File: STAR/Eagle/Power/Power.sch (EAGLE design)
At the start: 24 parts, among them J1 J30J-9J30, T1 750311838, U1 LT8300, U2 LT8330

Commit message: Power Board
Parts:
- removed D4: PMEG6010CEJ, AR_diode:SCHOTTKYSOD323
- removed T1: 750311838, AR_transformer:750311838
- added C10, C11, C12: .18 uF, resistor:C-USC0603
- added C13, C14, C15: 10 uF, resistor:C-USC0603
- added C16, C18, C20, C22, C24: KTJ500B476M76BFT00, Filtering:KTJ500B476M76BFT00
- added C17, C19, C21, C23, C25: 1nF, resistor:C-USC0603
- added C8, C9: .1 uF, resistor:C-USC0603
- added L2: 5.5u, Filtering:744325550
- added L3: 3.7u, Power:7443551370
- added L4, L5, L6, L7, L8: 744029000068, Filtering:744029000068
- added R9: 13.3k, resistor:R-US_R0603
- added U$1, U$2: DFT7160-105B, Filtering:DFT7160-105B
- added U3: LMR16020, HASP:LMR16020
- C1: value 22uF -> 10 uF; device AR_passives:CAPACITORC3025 -> resistor:C-USC1210
- C2: value 1uF -> 10 uF; device AR_passives:CAPACITORC0603 -> resistor:C-USC1210
- C3: value (none) -> 10 uF
- C4: value 10uF -> 2.2 uF; device AR_passives:CAPACITOR2-J-LEAD -> resistor:C-USC1210
- C5: value 1uF -> 2.2 uF; device AR_passives:CAPACITORC0603 -> resistor:C-USC1210
- C6: value 4.7pF -> 2.2 uF; device AR_passives:CAPACITORC0603 -> resistor:C-USC1210
- C7: value 1uF -> .1 uF; device AR_passives:CAPACITORC0603 -> resistor:C-USC0603
- D1: value MMSZ5266BT1G -> DO-214AC; device AR_diode:ZENERSOD123 -> HASP:DO-214AC
- D2: value BAV20W -> DO-214AC; device AR_diode:SCHOTTKYSOD323 -> HASP:DO-214AC
- D3: value SBR0560S1 -> DO-214AC; device AR_diode:SCHOTTKYSOD123 -> HASP:DO-214AC
- J1: value J30J-9J30 -> J30J-25; device CM_J30J:J30J-9J30 -> CM_J30J:J30J-25
- L1: value 10uH -> 9.7u; device AR_passives:INDUCTORPQ2614 -> Power:744314101
- R1: value 47k -> 23.2k; device resistor:R-US_R2512 -> resistor:R-US_R0603
- R2: value 407k -> 23.2k
- R3: value 1k -> 23.2k
- R4: value 3k -> 199.5k; device resistor:R-US_R2512 -> resistor:R-US_R0603
- R5: value 1.5k -> 13.3k; device resistor:R-US_R2512 -> resistor:R-US_R0603
- R6: value 1M -> 75.4k
- R7: value 33k -> 13.3k
- R8: value 52.6 -> 45.2k
- U1: value LT8300 -> LMR16020; device AR_IC:LT8300 -> HASP:LMR16020
- U2: value LT8330 -> LMR16020; device AR_IC:LT8330 -> HASP:LMR16020
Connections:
- removed net +20V: C3.1, C5.1, D3.C, L1.1, U2.EN, U2.VCC
- removed net +50V: C4.1, C6.1, D4.C, J1.1, J1.2, R1.2, R5.2, R6.2
- removed net N$11: R7.1, R8.2
- removed net VCC: C1.1, C2.1, D1.A, J1.4, T1.PA, U1.EN, U1.VCC
- removed net V_DIVIDE: J1.5, R1.1, R4.2
- new net +12V: C10.1, C13.1, L1.P$2, L8.P$1, R4.2
- new net +3V3: C12.1, C15.1, L3.P$2, L6.P$1, R8.2
- new net +5V: C11.1, C14.1, L2.P$2, L5.P$1, R6.2
- new net 12V_FILT: C24.P$1, C25.1, J1.3, L8.P$2
- new net 3V3_FILT: C20.P$1, C21.1, J1.1, L6.P$2
- new net 5V_FILT: C18.P$1, C19.1, J1.16, J1.18, J1.2, J1.8, L5.P$2
- new net D: J1.10
- new net ER: J1.12
- new net F: J1.6
- new net GSE_FILT: C16.P$1, C17.1, C2.1, C3.1, C5.1, C6.1, L4.P$2, U2.EN, U2.VIN, U3.EN, U3.VIN
- new net GSE_GND: C11.2, C12.2, C14.2, C15.2, C16.P$2, C17.2, C18.P$2, C19.2, C2.2, C20.P$2, C21.2, C3.2, C5.2, C6.2, D2.P$1, D3.P$1, J1.14, J1.17, J1.19, J1.20, J1.21, J1.22, R2.1, R3.1, R7.1, R9.1, U2.GND, U3.GND
- new net GSE_UFILT: J1.15, U$1.P$1, U$1.P$3
- new net I: J1.4
- new net N$14: C7.1, D1.P$2, L1.P$1, U1.SW
- new net N$27: R4.1, R5.2, U1.FB
- new net N$28: L4.P$1, U$1.P$2, U$1.P$4
- new net N$29: L7.P$1, U$2.P$2, U$2.P$4
- new net N$44: J1.25
- new net N$45: J1.24
- new net N$46: J1.23
- new net N$8: R8.1, R9.2, U3.FB
- new net Q: J1.7
- new net T: J1.5
- new net TE_FILT: C1.1, C22.P$1, C23.1, C4.1, L7.P$2, U1.EN, U1.VIN
- new net TE_UFILT: J1.13, U$2.P$1, U$2.P$3
- net GND: now also C10.2, C13.2, C22.P$2, C23.2, C24.P$2, C25.2, D1.P$1, J1.11, J1.9, R1.1; no longer C2.2, C3.2, C5.2, C7.2, J1.6, J1.7, R4.1, R8.1, T1.S2A, U2.GND
- net N$1: now also R3.2, U3.RT/SYNC; no longer D1.C, D2.C
- net N$10: now also C7.2, U1.BOOT; no longer J1.9
- net N$2: now also C9.1, D3.P$2, L3.P$1, U3.SW; no longer R2.1, U1.FB
- net N$3: now also U2.RT/SYNC; no longer R3.1
- net N$4: now also C8.2, U2.BOOT; no longer D2.A, R3.2, T1.PB, U1.SW
- net N$5: now also C8.1, D2.P$2, L2.P$1, U2.SW; no longer D3.A, T1.S2B
- net N$6: now also C9.2, U3.BOOT; no longer C7.1, U2.INTVCC
- net N$7: now also R1.2, U1.RT/SYNC; no longer D4.A, L1.2, U2.SW
- net N$9: no longer C6.2
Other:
- note added: "12 V Line"
- note added: "3.3 V Line"
- note added: "5 V Line"
- note added: "GSE Filter Network"
- note added: "TE Filter Network"
- note removed: "BOOST STAGE"
- note removed: "ISOLATION STAGE"
- note removed: "Voltage Divider"
- moved on the sheet: C1, C2, C3, C4, C5, C6, C7, R1, R2, R3, R4, R5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

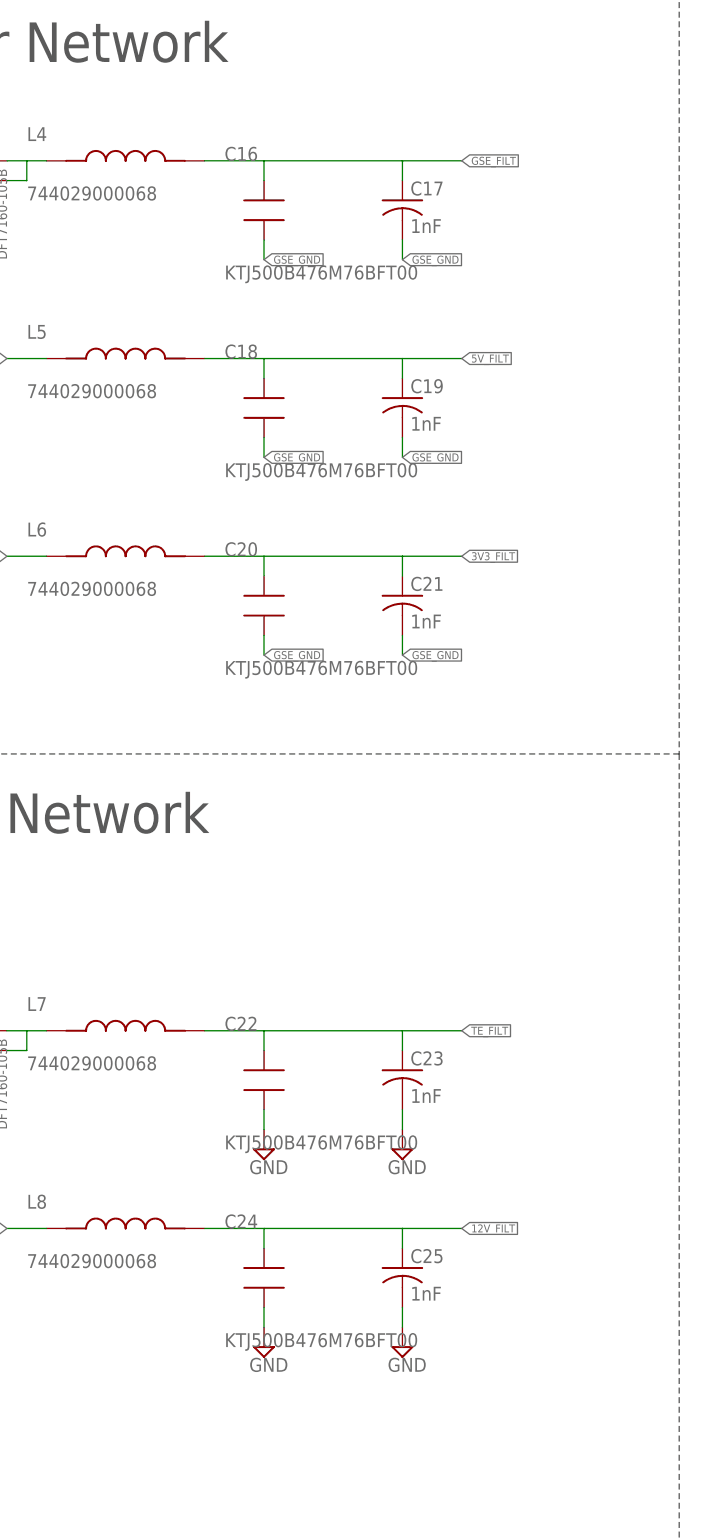
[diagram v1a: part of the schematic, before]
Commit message: new filtering caps for power board
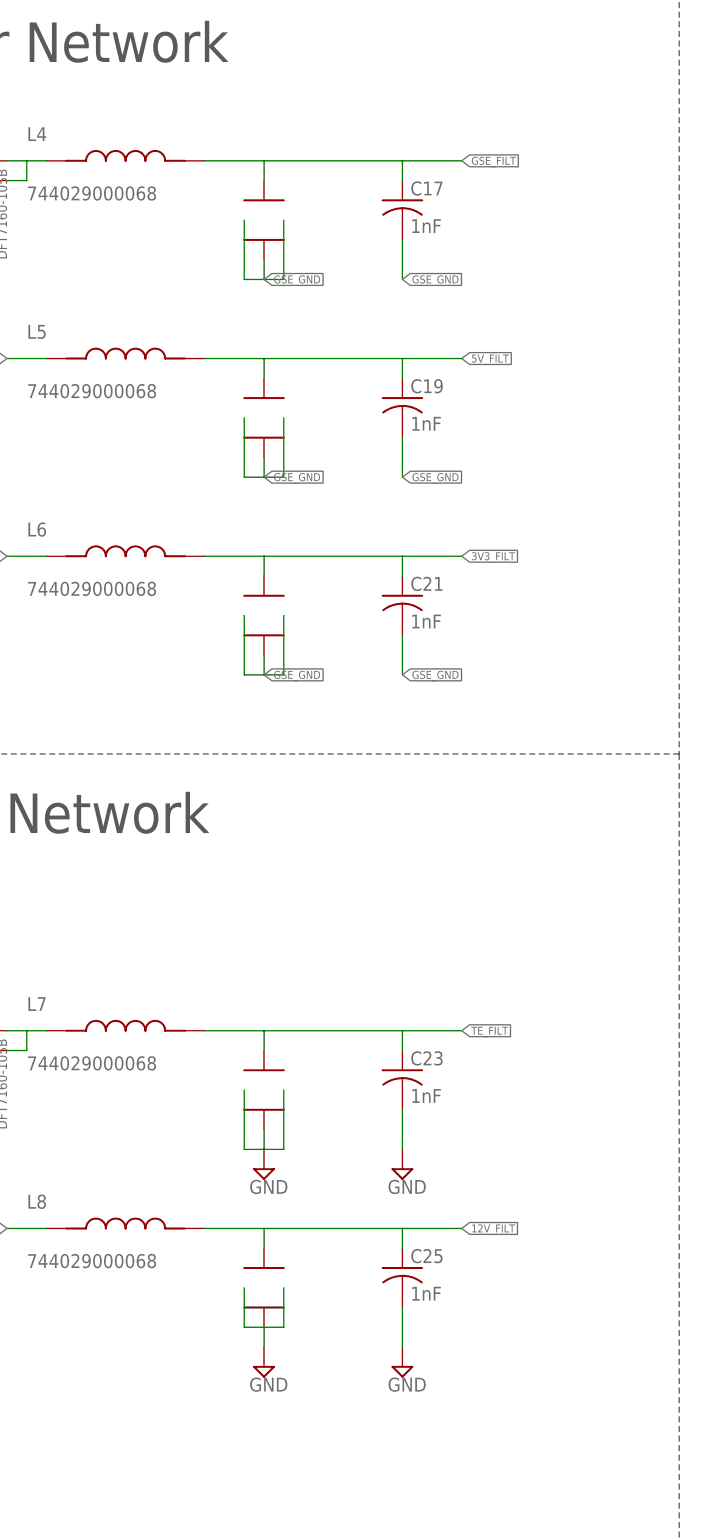
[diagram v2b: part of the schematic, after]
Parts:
- removed C16, C18, C20, C22, C24: KTJ500B476M76BFT00, Filtering:KTJ500B476M76BFT00
- added U$3, U$4, U$5, U$6, U$7: 1410J0500404MXTE03, Filtering:1410J0500404MXTE03
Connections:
- net 12V_FILT: now also U$7.P$2; no longer C24.P$1
- net 3V3_FILT: now also U$5.P$2; no longer C20.P$1
- net 5V_FILT: now also U$4.P$2; no longer C18.P$1
- net GND: now also U$6.P$1, U$6.P$3, U$6.P$4, U$7.P$1, U$7.P$3, U$7.P$4; no longer C22.P$2, C24.P$2
- net GSE_FILT: now also U$3.P$2; no longer C16.P$1
- net GSE_GND: now also U$3.P$1, U$3.P$3, U$3.P$4, U$4.P$1, U$4.P$3, U$4.P$4, U$5.P$1, U$5.P$3, U$5.P$4; no longer C16.P$2, C18.P$2, C20.P$2
- net TE_FILT: now also U$6.P$2; no longer C22.P$1

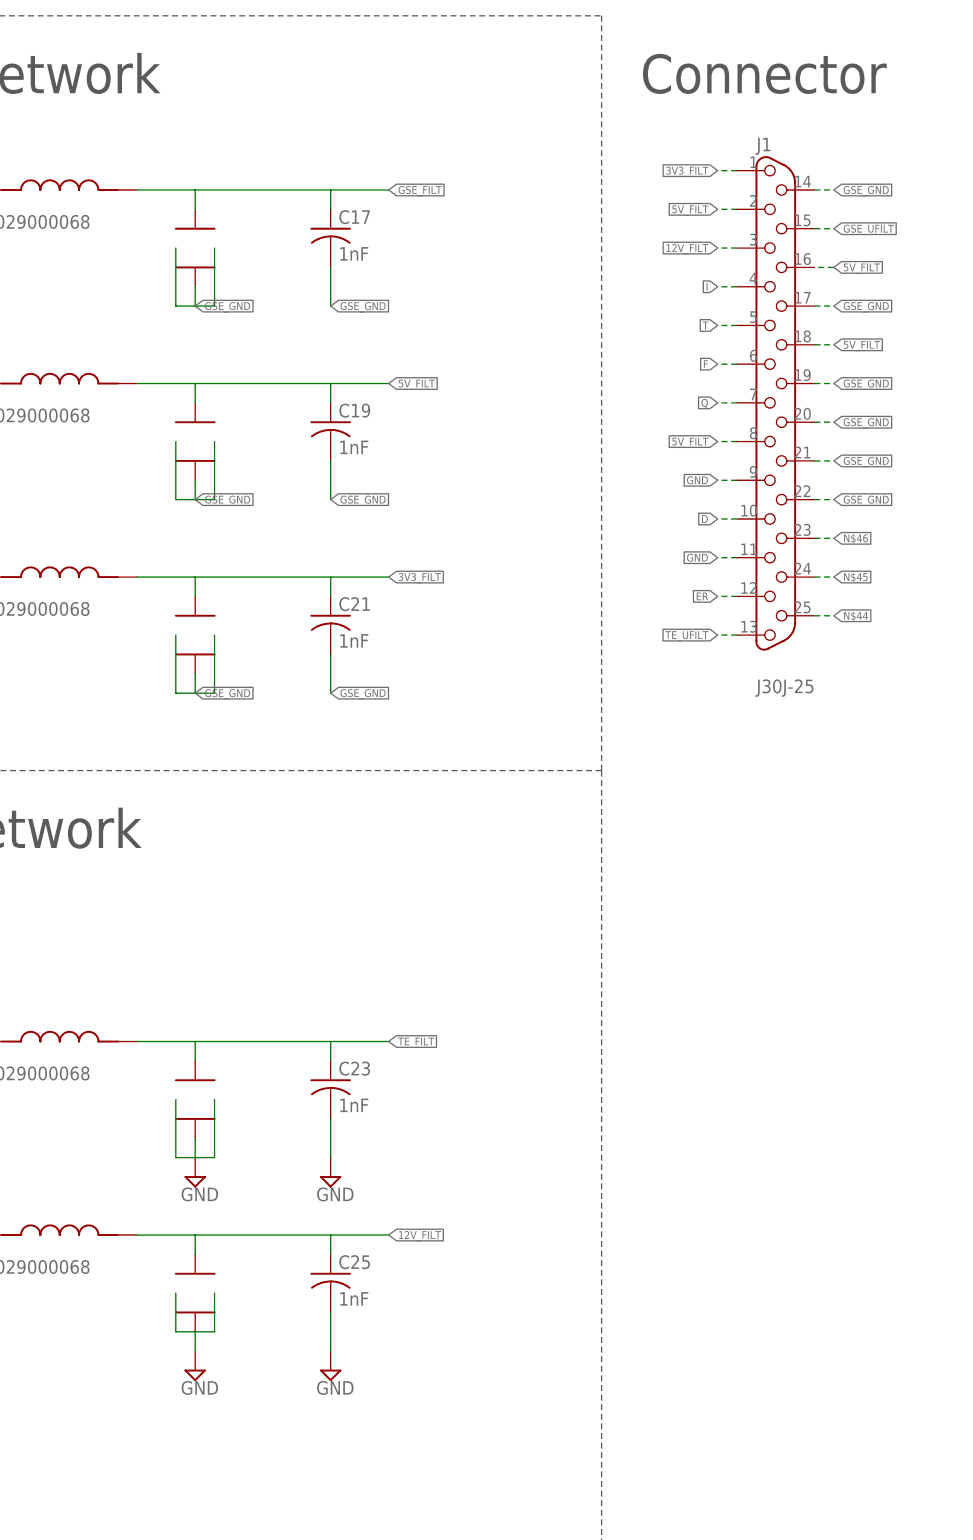
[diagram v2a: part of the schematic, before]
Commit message: Fixed the three terminal capacitor routing (five capacitors).
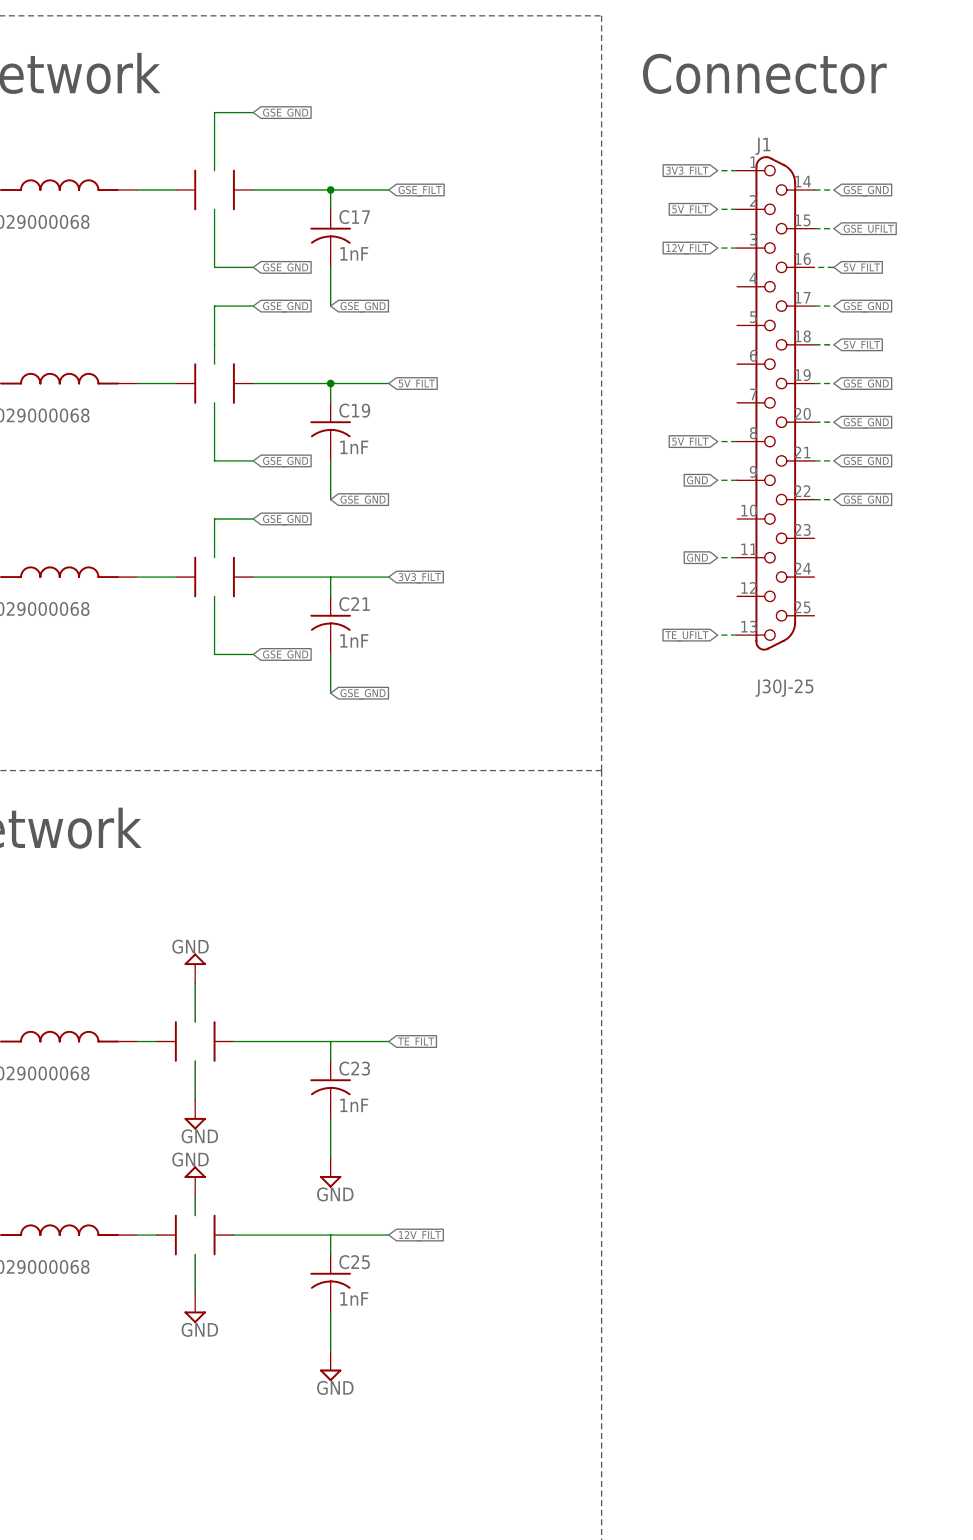
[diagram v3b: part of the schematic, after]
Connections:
- removed net D: J1.10
- removed net ER: J1.12
- removed net F: J1.6
- removed net I: J1.4
- removed net N$44: J1.25
- removed net N$45: J1.24
- removed net N$46: J1.23
- removed net Q: J1.7
- removed net T: J1.5
- new net N$31: L4.P$2, U$3.P$2
- new net N$32: L5.P$2, U$4.P$2
- new net N$33: L6.P$2, U$5.P$1
- new net N$34: L7.P$2, U$6.P$1
- new net N$35: L8.P$2, U$7.P$1
- net 12V_FILT: no longer L8.P$2
- net 3V3_FILT: no longer L6.P$2
- net 5V_FILT: now also U$4.P$1; no longer L5.P$2, U$4.P$2
- net GND: no longer U$6.P$1, U$7.P$1
- net GSE_FILT: now also U$3.P$1; no longer L4.P$2, U$3.P$2
- net GSE_GND: no longer U$3.P$1, U$4.P$1, U$4.P$3, U$4.P$4, U$5.P$1
- net TE_FILT: no longer L7.P$2
